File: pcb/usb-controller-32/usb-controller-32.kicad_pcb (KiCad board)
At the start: 2 copper layers, 93 parts, among them J1 USB_MiniB_Adafruit_Breakout, J2 Conn_01x08_Pin, J3 Conn_01x03_Pin, SW1 SW_Push_Dual, SW10 SW_Push_Dual, SW11 SW_Push_Dual, SW12 SW_Push_Dual, SW13 SW_Push_Dual, SW14 SW_Push_Dual, SW15 SW_Push_Dual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

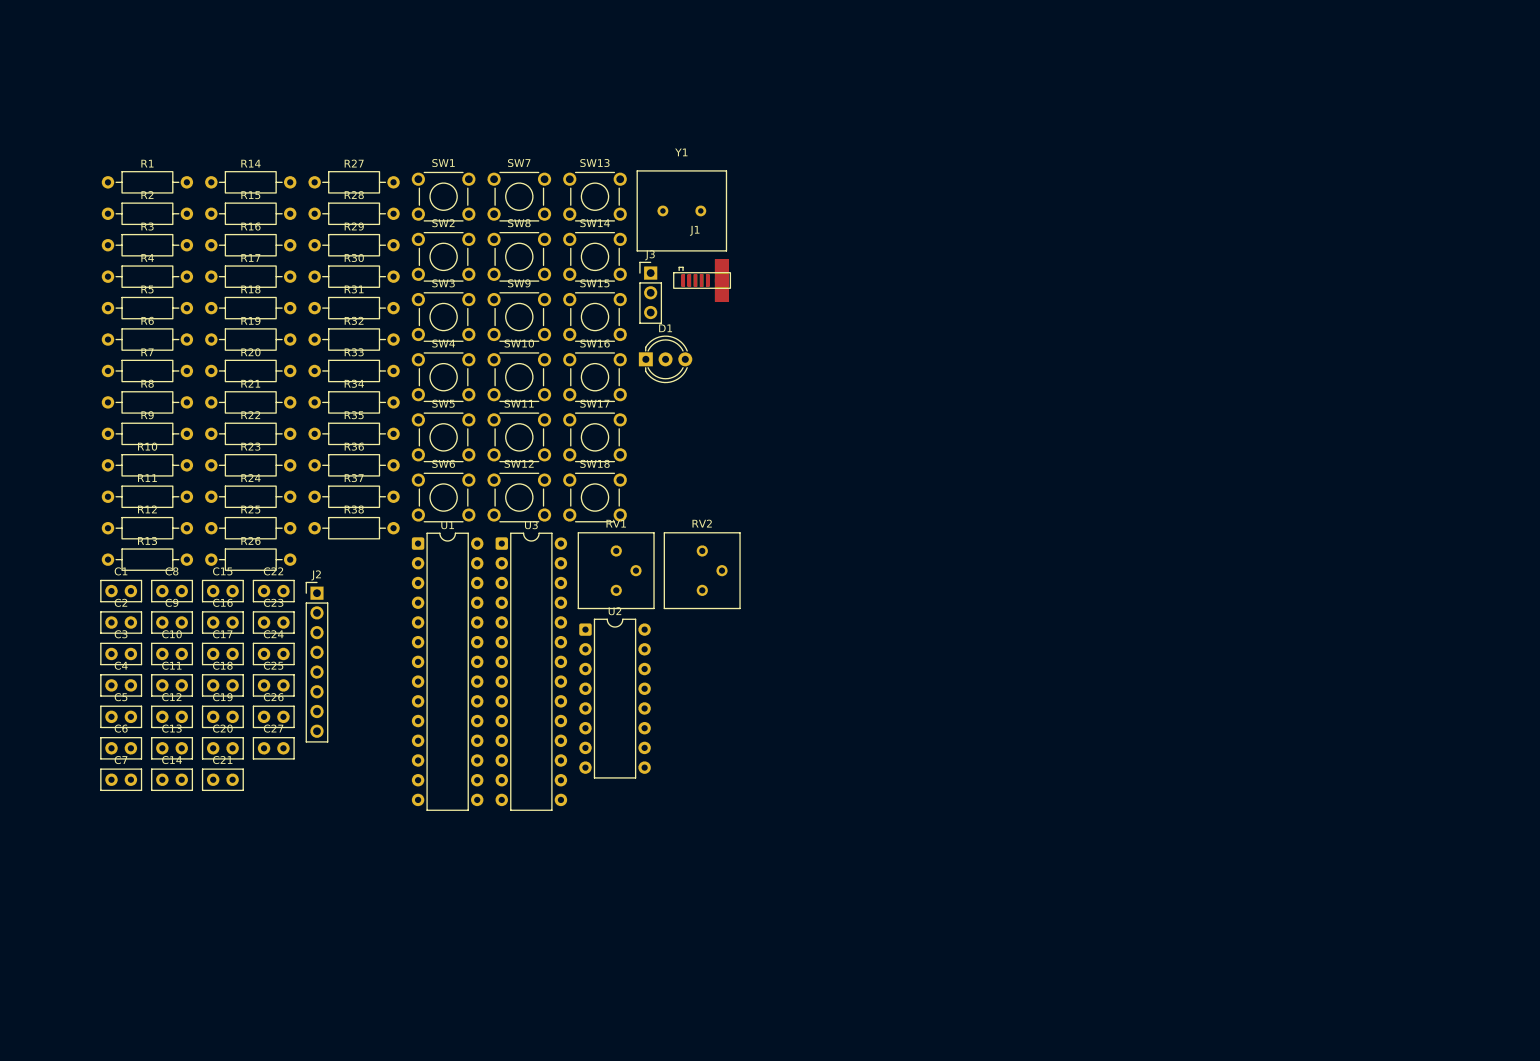
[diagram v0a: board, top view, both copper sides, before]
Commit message: add claude generated python script to layout pcb add resulting pcb of aformentioned script run
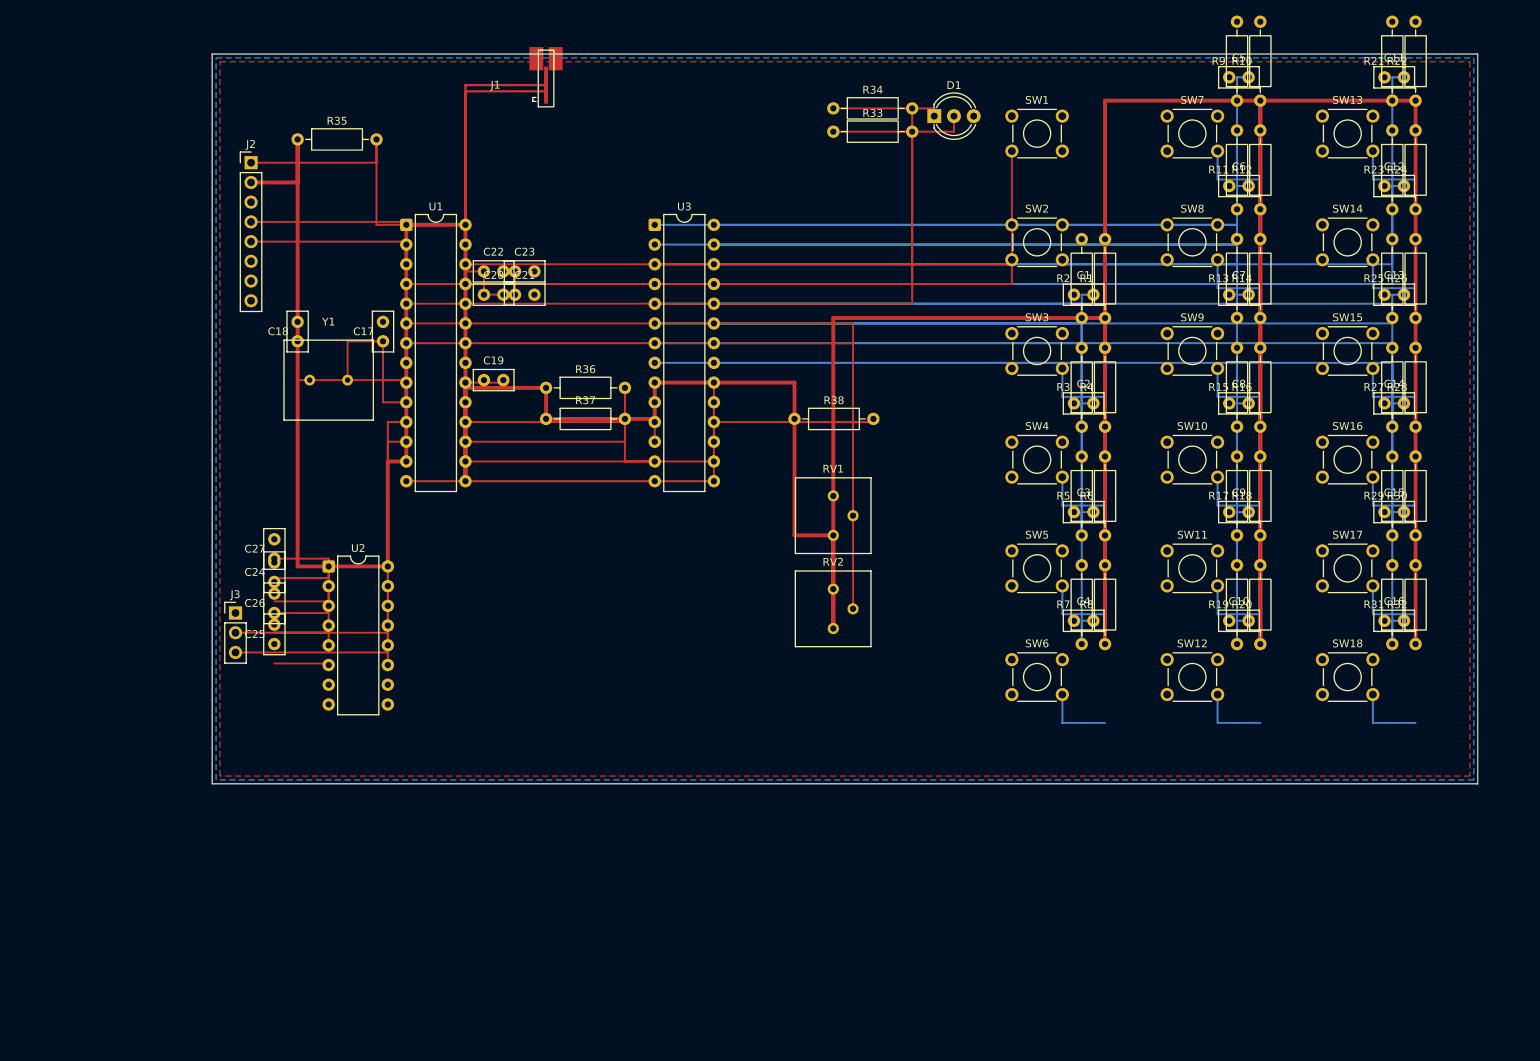
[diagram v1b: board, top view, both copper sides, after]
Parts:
- moved C11 175.8 mm to (236.0, 29.0)
- moved C12 171.6 mm to (236.0, 43.0)
- moved C13 167.9 mm to (236.0, 57.0)
- moved C5 165.9 mm to (216.0, 29.0)
- moved C14 164.7 mm to (236.0, 71.0)
- moved C6 161.2 mm to (216.0, 43.0)
- moved R22 160.9 mm to (240.0, 32.0), turned to 90 degrees
- moved R24 159.5 mm to (240.0, 46.0), turned to 90 degrees
- moved R26 158.2 mm to (240.0, 60.0), turned to 90 degrees
- moved R21 157.0 mm to (237.0, 32.0), turned to 90 degrees
- moved C7 156.9 mm to (216.0, 57.0)
- moved R10 155.7 mm to (220.0, 32.0), turned to 90 degrees
- moved R23 155.6 mm to (237.0, 46.0), turned to 90 degrees
- moved R25 154.5 mm to (237.0, 60.0), turned to 90 degrees
- moved R12 154.0 mm to (220.0, 46.0), turned to 90 degrees
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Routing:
- net +5V: track 0.00 -> 701.9 mm
- net /GPB7: track 0.00 -> 135.7 mm
- net /GPB1: track 0.00 -> 131.0 mm
- net /GPB6: track 0.00 -> 124.3 mm
- net /GPB2: track 0.00 -> 120.6 mm
- net /GPB0: track 0.00 -> 119.5 mm
- net /GPB5: track 0.00 -> 112.8 mm
- net /GPB3: track 0.00 -> 109.1 mm
- net /GPB4: track 0.00 -> 101.3 mm
- net /GPA7: track 0.00 -> 97.9 mm
- net /GPA3: track 0.00 -> 95.7 mm
- net /GPA4: track 0.00 -> 95.5 mm
- net /POT_2: track 0.00 -> 91.8 mm
- net /GREEN_LED: track 0.00 -> 87.8 mm
- net /BTN1: track 0.00 -> 87.5 mm
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- added copper zone on F.Cu, net +5V
- added copper zone on B.Cu, net GND
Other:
- board outline added: 163 x 94 mm

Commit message: update pcb replace led footprint with gnd in middle
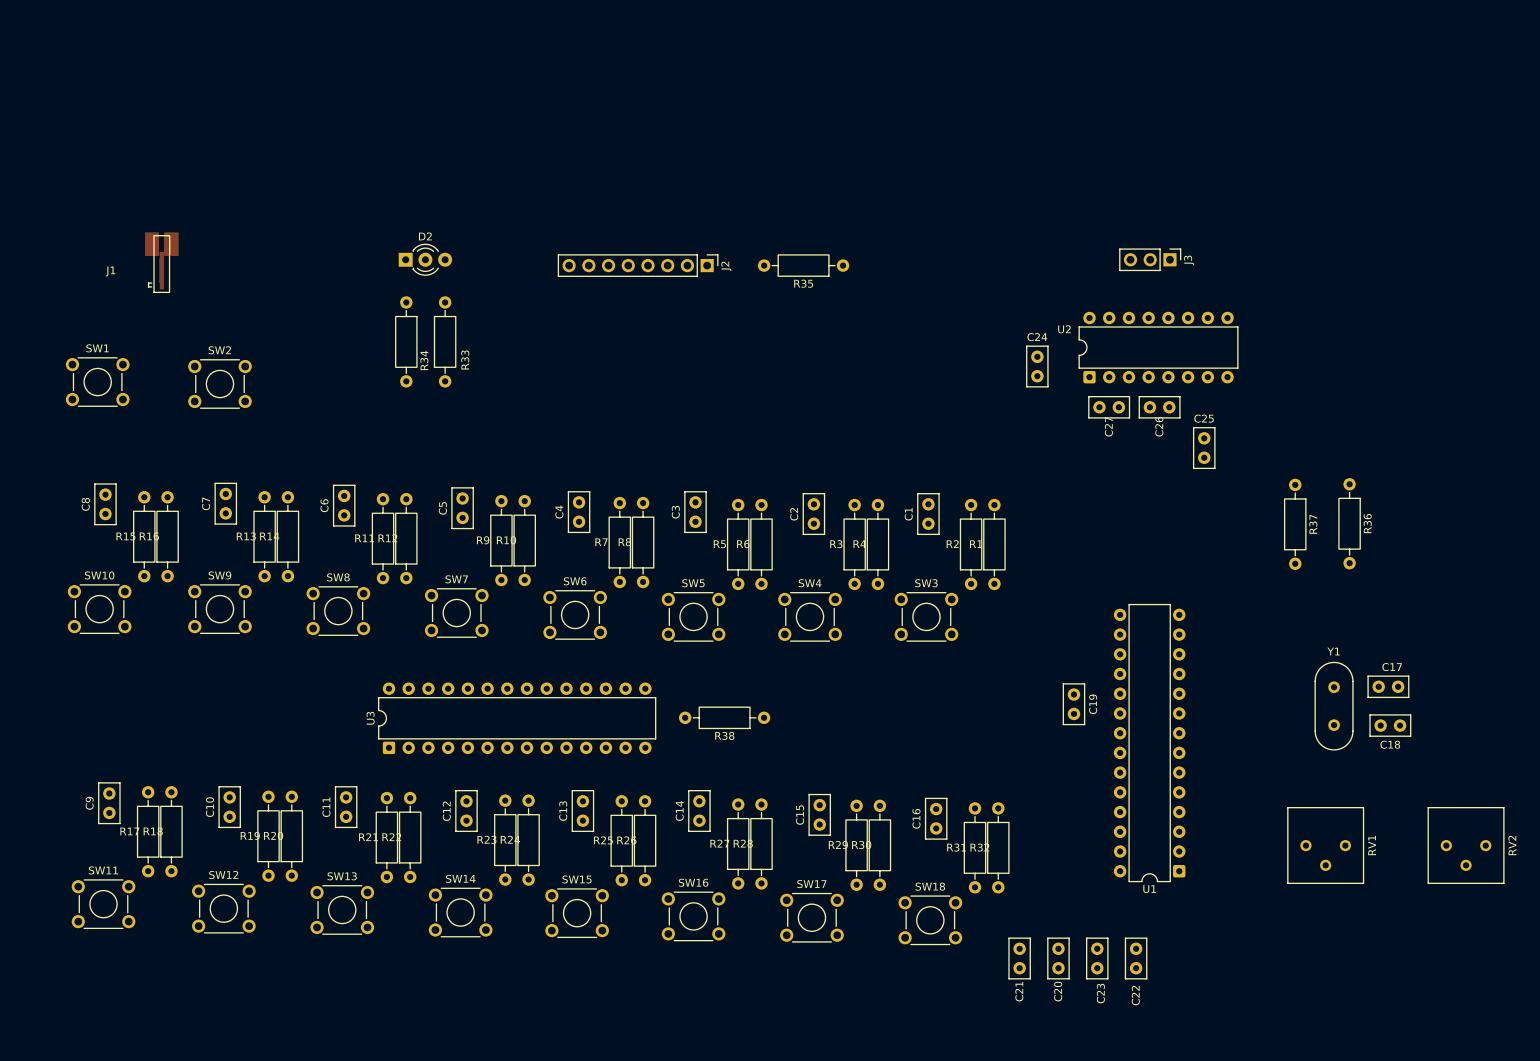
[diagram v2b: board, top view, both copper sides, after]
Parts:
- removed D1: LED_Dual_AAK, LED_THT:LED_D5.0mm-3
- added D2: LED_Dual_AKA, LED_THT:LED_D3.0mm-3, F.Cu at (109.9, 52.5)
- Y1: footprint extra:Crystal_HC49-U_Vertical_20MHz -> Crystal:Crystal_HC49-4H_Vertical
- moved C11 164.2 mm to (102.2, 124.2), turned to 90 degrees
- moved R21 163.6 mm to (107.5, 132.0)
- moved R22 163.6 mm to (110.5, 132.0)
- moved SW13 163.6 mm to (98.5, 134.0)
- moved C18 150.4 mm to (238.0, 112.5), turned to 180 degrees
- moved C9 149.4 mm to (71.8, 123.8), turned to 90 degrees
- moved R17 146.8 mm to (76.8, 131.2)
- moved R18 146.8 mm to (79.8, 131.2)
- moved SW11 146.8 mm to (67.8, 133.2)
- moved C8 145.4 mm to (71.2, 85.2), turned to 90 degrees
- moved C12 143.8 mm to (117.8, 124.8), turned to 90 degrees
- moved R23 143.2 mm to (122.8, 132.3)
- moved R24 143.2 mm to (125.8, 132.3)
- moved SW14 143.2 mm to (113.8, 134.3)
- moved R15 142.1 mm to (76.2, 93.2)
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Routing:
- net +5V: track 701.9 -> 0.00 mm
- net /GPB7: track 135.7 -> 0.00 mm
- net /GPB1: track 131.0 -> 0.00 mm
- net /GPB6: track 124.3 -> 0.00 mm
- net /GPB2: track 120.6 -> 0.00 mm
- net /GPB0: track 119.5 -> 0.00 mm
- net /GPB5: track 112.8 -> 0.00 mm
- net /GPB3: track 109.1 -> 0.00 mm
- net /GPB4: track 101.3 -> 0.00 mm
- net /GPA7: track 97.9 -> 0.00 mm
- net /GPA3: track 95.7 -> 0.00 mm
- net /GPA4: track 95.5 -> 0.00 mm
- net /POT_2: track 91.8 -> 0.00 mm
- net /GREEN_LED: track 87.8 -> 0.00 mm
- net /BTN1: track 87.5 -> 0.00 mm
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- removed copper zone on F.Cu, net +5V
- removed copper zone on B.Cu, net GND
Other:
- board outline removed

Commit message: add routed pcb
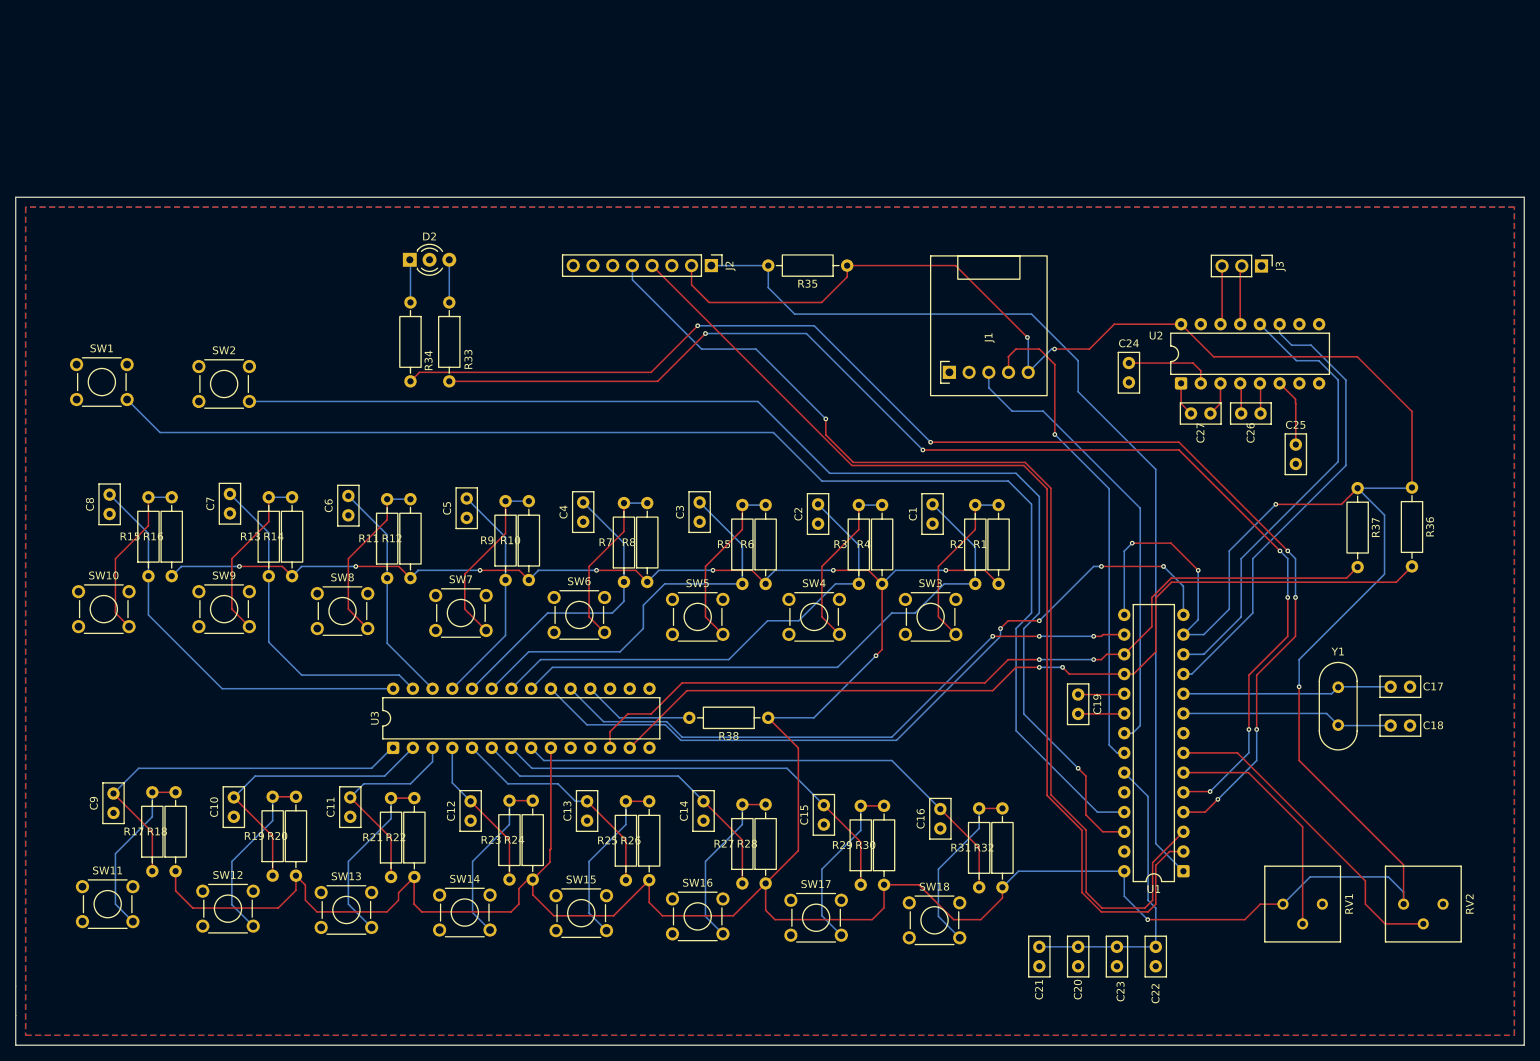
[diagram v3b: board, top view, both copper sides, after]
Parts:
- moved J1 107.3 mm to (185.0, 67.0), turned to 0 degrees
- moved C24 11.8 mm to (203.1, 68.3)
- moved C25 11.8 mm to (224.6, 78.8)
- moved C27 11.8 mm to (213.6, 72.3)
- moved J3 11.8 mm to (220.2, 53.3)
- moved U2 11.8 mm to (209.8, 68.4)
- moved C26 11.8 mm to (220.0, 72.3)
- moved R33 10.2 mm to (115.5, 58.0), turned to -90 degrees
- moved RV2 9.34 mm to (238.5, 135.5)
- moved RV1 8.10 mm to (222.9, 135.5)
- moved R36 8.05 mm to (239.5, 81.8)
- moved R37 8.05 mm to (232.5, 81.9)
- moved C20 2.55 mm to (196.5, 141.0)
- moved C21 2.55 mm to (191.5, 141.0)
- moved C22 2.55 mm to (206.5, 141.0)
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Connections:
- J1 pad 5: +3.3V -> +5V
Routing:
- net +5V: track 0.00 -> 654.0 mm, vias 0 -> 15
- net /BTN1: track 0.00 -> 170.4 mm
- net /GREEN_LED: track 0.00 -> 169.7 mm, vias 0 -> 6
- net /RED_LED: track 0.00 -> 160.2 mm, vias 0 -> 6
- net /BTN2: track 0.00 -> 157.8 mm, vias 0 -> 1
- net /PGEC1: track 0.00 -> 142.3 mm, vias 0 -> 1
- net /PGED1: track 0.00 -> 137.0 mm
- net /MCLR: track 0.00 -> 125.4 mm
- net /SDA: track 0.00 -> 115.2 mm, vias 0 -> 2
- net /SCL: track 0.00 -> 109.4 mm, vias 0 -> 2
- net /INTA: track 0.00 -> 98.8 mm, vias 0 -> 4
- net /INTB: track 0.00 -> 79.4 mm, vias 0 -> 3
- net /GPA0: track 0.00 -> 75.3 mm
- net /GPB7: track 0.00 -> 68.1 mm
- net /USB_DM: track 0.00 -> 63.5 mm, vias 0 -> 1
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- added copper zone on B.Cu, net GND
- added copper zone on F.Cu, net GND
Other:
- board outline added: 194.3 x 109.2 mm
